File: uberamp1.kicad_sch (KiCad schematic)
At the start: 14 parts

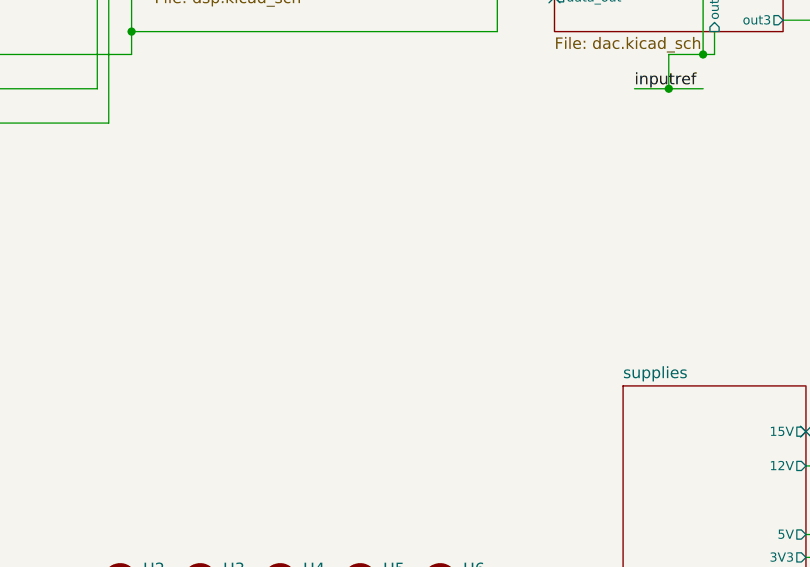
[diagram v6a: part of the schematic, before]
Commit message: add fan control circuit
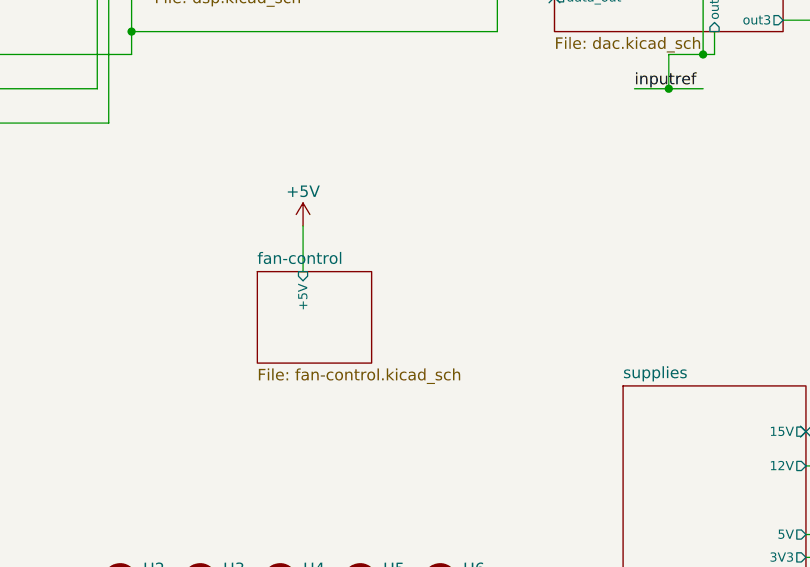
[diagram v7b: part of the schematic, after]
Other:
- added sheet fan-control (fan-control.kicad_sch)
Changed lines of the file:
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@@
 	(wire
 		(pts
+			(xy 101.6 148.59) (xy 101.6 153.67)
+		)
+		(stroke
+			(width 0)
+			(type default)
+		)
+	)
+	(wire
+		(pts
 			(xy 142.24 58.42) (xy 142.24 55.88)
 		)
@@
 	)
 	(symbol
+		(lib_id "power:+5V")
+		(at 101.6 148.59 0)
+		(unit 1)
+		(exclude_from_sim no)
+		(in_bom yes)
+		(on_board yes)
+		(dnp no)
+		(fields_autoplaced yes)
+		(property "Reference" "#PWR0208"
+			(at 101.6 152.4 0)
+			(effects
+				(font
+					(size 1.27 1.27)
+				)
+				(hide yes)
+			)
+		)
+		(property "Value" "+5V"
+			(at 101.6 144.78 0)
+			(effects
+				(font
+					(size 1.27 1.27)
+				)
+			)
+		)
+		(property "Footprint" ""
+			(at 101.6 148.59 0)
+			(effects
+				(font
+					(size 1.27 1.27)
+				)
+				(hide yes)
+			)
+		)
+		(property "Datasheet" ""
+			(at 101.6 148.59 0)
+			(effects
+				(font
+					(size 1.27 1.27)
+				)
+				(hide yes)
+			)
+		)
+		(property "Description" ""
+			(at 101.6 148.59 0)
+			(effects
+				(font
+					(size 1.27 1.27)
+				)
+				(hide yes)
+			)
+		)
+		(pin "1"
+		)
+		(instances
+			(project "uberamp1"
+				(path "/310059c1-d84b-43e2-9c9a-0e426c534a12"
+					(reference "#PWR0208")
+					(unit 1)
+				)
+			)
+		)
+	)
+	(symbol
 		(lib_id "Mechanical:MountingHole_Pad")
 		(at 99.06 189.23 0)
@@
 				)
 			)
+		)
+	)
+	(sheet
+		(at 96.52 153.67)
+		(size 12.7 10.16)
+		(fields_autoplaced yes)
+		(stroke
+			(width 0.1524)
+			(type solid)
+		)
+		(fill
+			(color 0 0 0 0.0000)
+		)
+		(property "Sheetname" "fan-control"
+			(at 96.52 152.9584 0)
+			(effects
+				(font
+					(size 1.27 1.27)
+				)
+				(justify left bottom)
+			)
+		)
+		(property "Sheetfile" "fan-control.kicad_sch"
+			(at 96.52 164.4146 0)
+			(effects
+				(font
+					(size 1.27 1.27)
+				)
+				(justify left top)
+			)
+		)
+		(pin "+5V" input
+			(at 101.6 153.67 90)
+			(effects
+				(font
+					(size 1.016 1.016)
+				)
+				(justify right)
+			)
+		)
+		(instances
+			(project "uberamp1"
+				(path "/310059c1-d84b-43e2-9c9a-0e426c534a12"
+					(page "23")
+				)
+			)

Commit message: all known bugs fixed
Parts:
- added TP10, TP11, TP12, TP16, TP17, TP18, TP19, TP23, TP24, TP9: gnd, invendelirium_audio:output_pad, symbol Connector:TestPoint
- added TP13, TP14, TP15, TP20, TP21, TP22: ~, invendelirium_audio:output_pad, symbol Connector:TestPoint
- added s48, s49, s50: gnd, invendelirium_general:pad_1.2x1.5, symbol Connector:TestPoint
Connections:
- net GND: now also TP10.1, TP11.1, TP12.1, TP16.1, TP17.1, TP18.1, TP19.1, TP23.1, TP24.1, TP9.1, s48.1, s49.1, s50.1
- no-connect marks 6 -> 12
